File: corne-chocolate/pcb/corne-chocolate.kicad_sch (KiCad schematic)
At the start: 74 parts, among them J1 MJ-4PP-9, J2 Conn_01x04, J3 Conn_01x03, P1 Conn_01x01, P2 Conn_01x01, SW10 SW_PUSH, SW11 SW_PUSH, SW12 SW_PUSH, SW14 SW_PUSH, SW15 SW_PUSH, SW16 SW_PUSH, SW17 SW_PUSH, SW18 SW_PUSH, SW19 SW_PUSH, SW2 SW_PUSH, SW20 SW_PUSH, SW21 SW_PUSH, SW3 SW_PUSH, SW4 SW_PUSH, SW5 SW_PUSH, SW6 SW_PUSH, SW8 SW_PUSH, SW9 SW_PUSH, U1 ProMicro

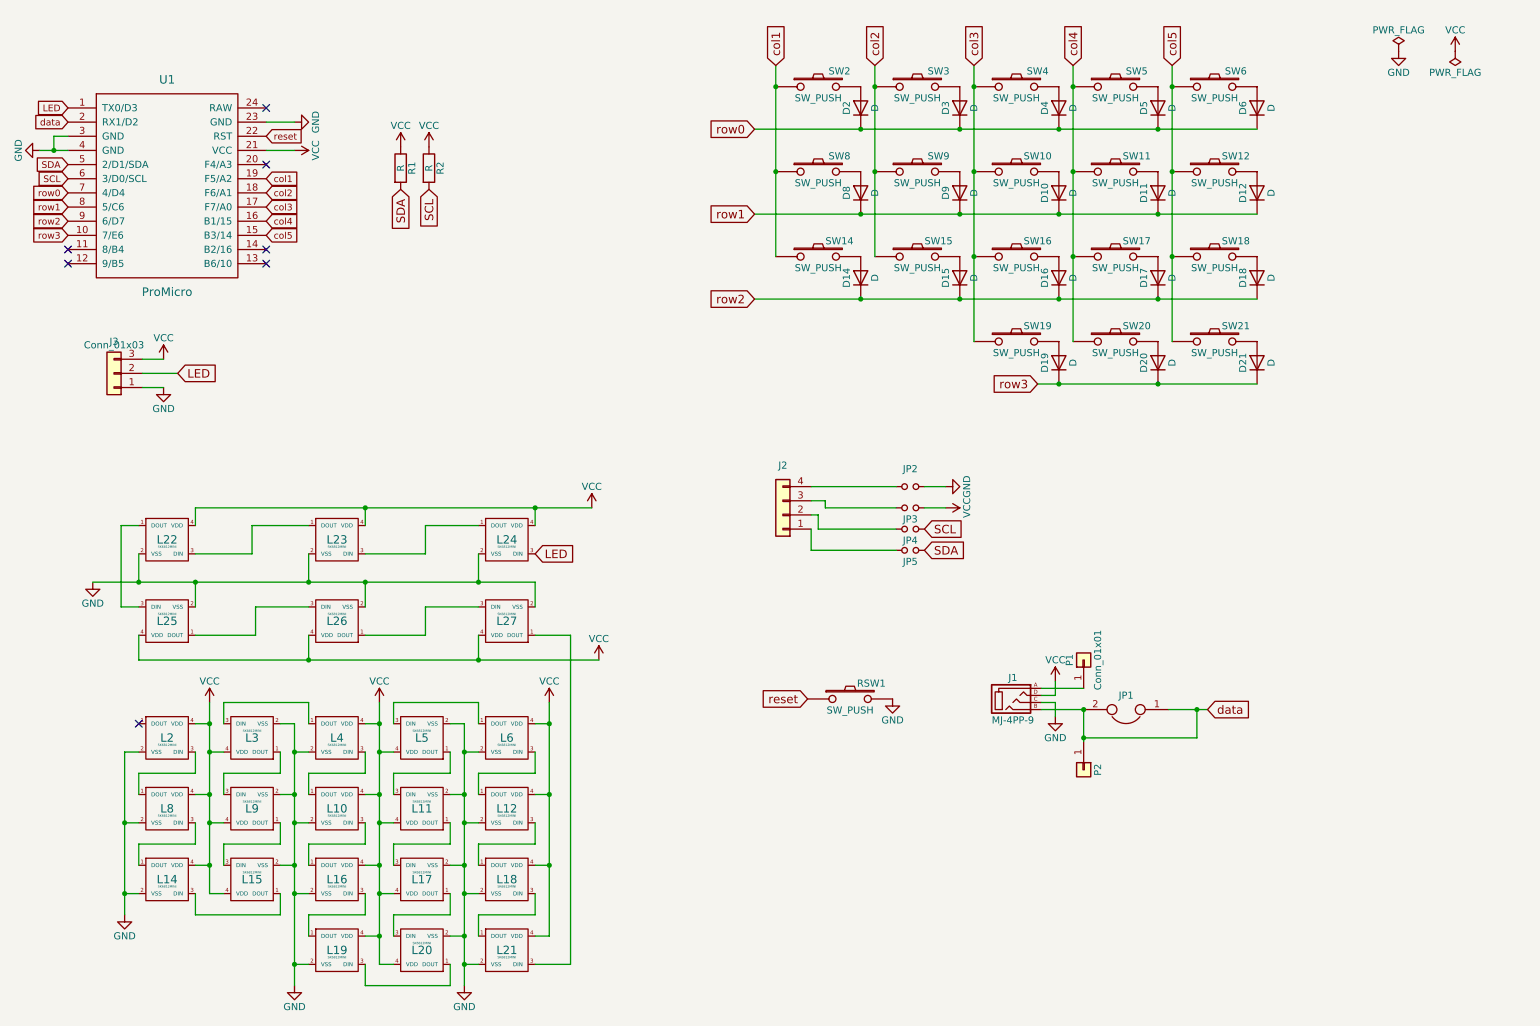
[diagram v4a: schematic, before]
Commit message: pcb with ohspark constraints
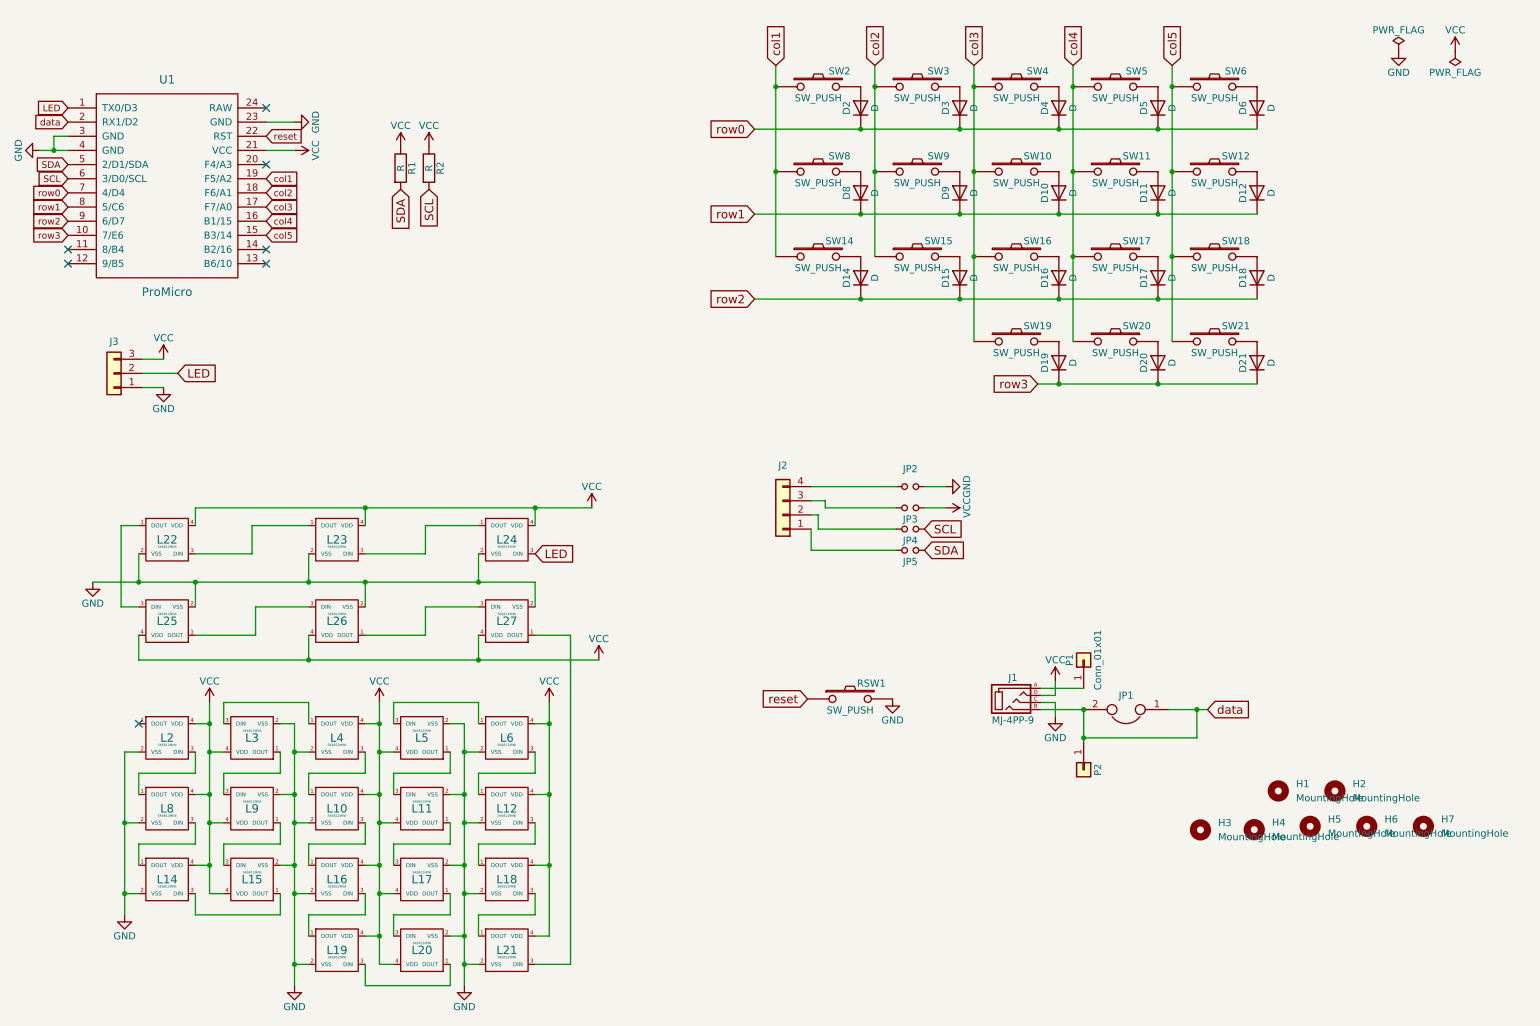
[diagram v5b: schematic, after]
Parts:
- added H1, H2: MountingHole, MountingHole:MountingHole_2.2mm_M2_ISO14580, symbol Mechanical:MountingHole
- added H3, H4, H5, H6, H7: MountingHole, MountingHole:MountingHole_4.3mm_M4_ISO14580, symbol Mechanical:MountingHole
- L10, L11, L12, L14, L15, L16, L17, L18, L19, L2, L20, L21, L3, L4, L5, L6, L8, L9: footprint kbd:SK6812MINI_rev -> kbd:YS-SK6812MINI-E

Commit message: finishes routing
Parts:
- SW10, SW11, SW12, SW14, SW15, SW16, SW17, SW18, SW19, SW2, SW20, SW21, SW3, SW4, SW5, SW6, SW8, SW9: supplier (none) -> Digikey; supplier pn (none) -> 1528-5118-ND
- U1: supplier (none) -> Digikey; supplier pn (none) -> 1568-DEV-15795-ND

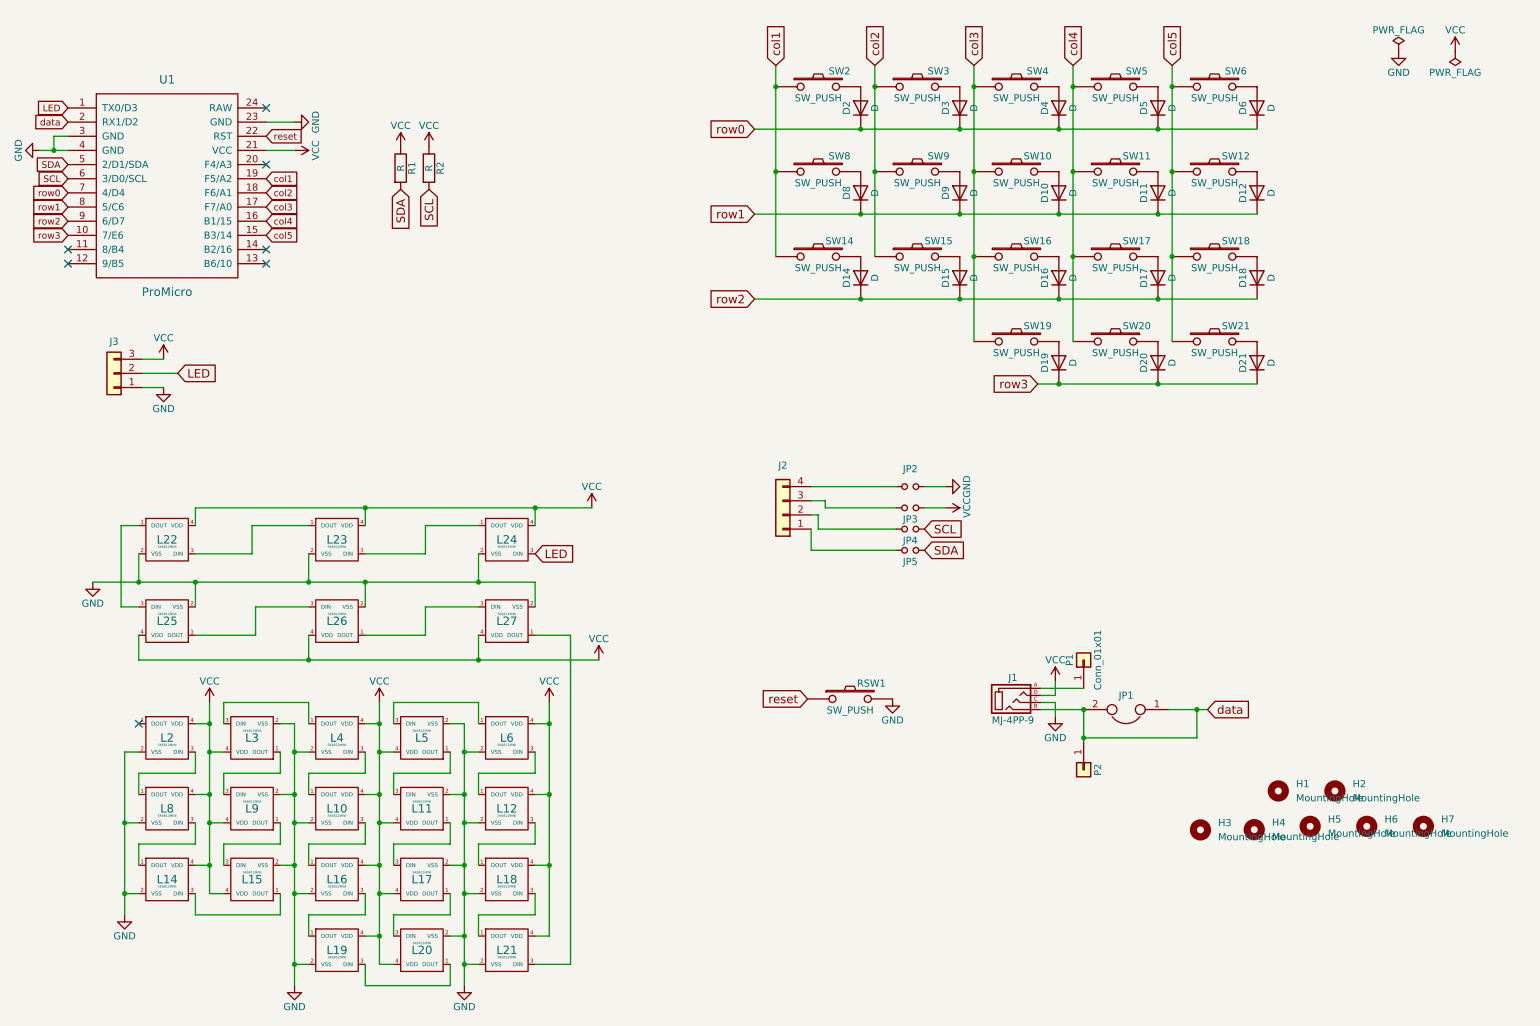
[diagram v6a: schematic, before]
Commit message: updates some footprints
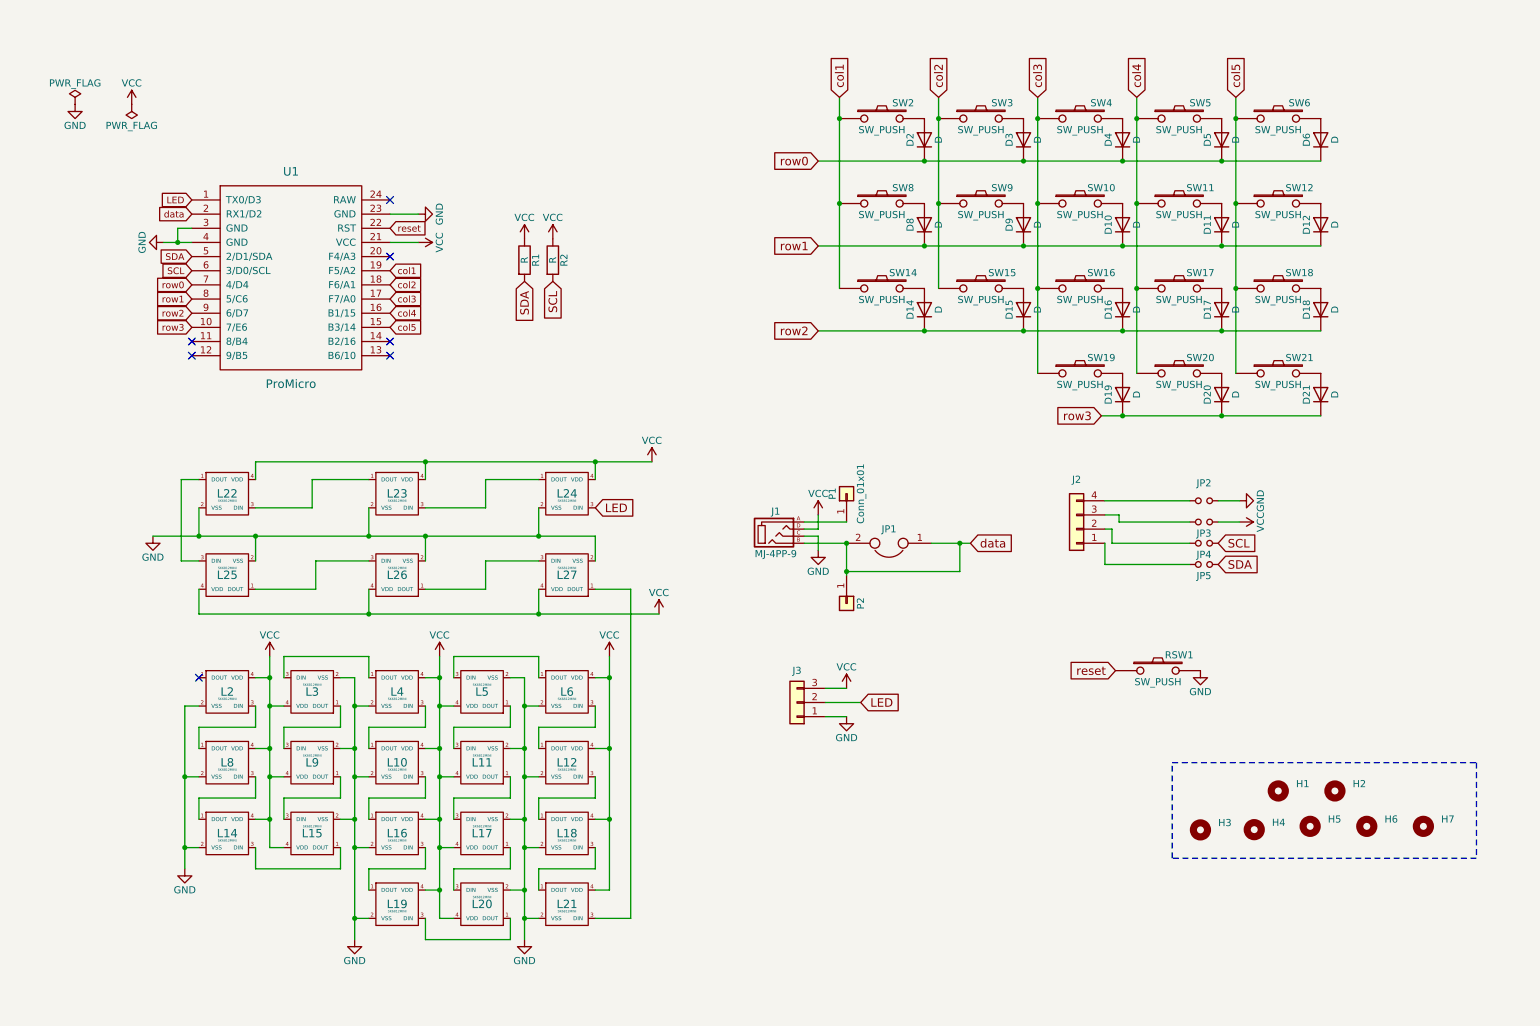
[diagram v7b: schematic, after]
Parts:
- SW14: footprint kbd:ChocV1_V2_Hotswap -> (none); supplier Digikey -> (none); supplier pn 1528-5118-ND -> (none)
- U1: footprint kbd:ProMicro_v2_1side -> (none); supplier Digikey -> (none); supplier pn 1568-DEV-15795-ND -> (none)
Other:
- moved on the sheet: D10, D11, D12, D14, D15, D16, D17, D18, D19, D2, D20, D21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

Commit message: reannotates
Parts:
- removed J3: Conn_01x03, kbd:StripLED_1side, symbol Connector_Generic:Conn_01x03
- removed JP1: Device:Jumper, kbd:Jumper, symbol kbd:Jumper-Device
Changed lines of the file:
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@@
   (junction (at 94.615 145.415) (diameter 0) (color 0 0 0 0)
   )
+  (junction (at 167.64 108.585) (diameter 0) (color 0 0 0 0)
+  )
   (junction (at 79.375 145.415) (diameter 0) (color 0 0 0 0)
   )
@@
   (junction (at 94.615 163.195) (diameter 0) (color 0 0 0 0)
   )
-  (junction (at 187.96 108.585) (diameter 0) (color 0 0 0 0)
-  )
   (junction (at 109.855 170.815) (diameter 0) (color 0 0 0 0)
   )
@@
   (junction (at 201.93 47.625) (diameter 0) (color 0 0 0 0)
   )
-  (junction (at 167.64 108.585) (diameter 0) (color 0 0 0 0)
-  )
   (junction (at 94.615 132.715) (diameter 0) (color 0 0 0 0)
   )
   (junction (at 92.075 107.315) (diameter 0) (color 0 0 0 0)
   )
-  (junction (at 167.64 113.665) (diameter 0) (color 0 0 0 0)
-  )
   (junction (at 217.17 55.245) (diameter 0) (color 0 0 0 0)
   )
@@
     (stroke (width 0) (type default))
   )
-  (wire (pts (xy 167.64 113.665) (xy 167.64 114.3))
+  (wire (pts (xy 167.64 108.585) (xy 167.64 114.3))
     (stroke (width 0) (type default))
   )
@@
     (stroke (width 0) (type default))
   )
-  (wire (pts (xy 167.64 108.585) (xy 167.64 113.665))
-    (stroke (width 0) (type default))
-  )
   (wire (pts (xy 92.075 154.305) (xy 92.075 150.495))
     (stroke (width 0) (type default))
@@
     (stroke (width 0) (type default))
   )
-  (wire (pts (xy 187.96 108.585) (xy 182.88 108.585))
+  (wire (pts (xy 167.64 108.585) (xy 174.625 108.585))
     (stroke (width 0) (type default))
   )
@@
     (stroke (width 0) (type default))
   )
-  (wire (pts (xy 163.83 134.62) (xy 167.64 134.62))
-    (stroke (width 0) (type default))
-  )
   (wire (pts (xy 112.395 170.815) (xy 112.395 167.005))
     (stroke (width 0) (type default))
@@
     (stroke (width 0) (type default))
   )
-  (wire (pts (xy 187.96 113.665) (xy 167.64 113.665))
-    (stroke (width 0) (type default))
-  )
   (wire (pts (xy 76.835 158.115) (xy 79.375 158.115))
     (stroke (width 0) (type default))
@@
     (stroke (width 0) (type default))
   )
-  (wire (pts (xy 163.83 137.16) (xy 170.18 137.16))
-    (stroke (width 0) (type default))
-  )
   (wire (pts (xy 79.375 150.495) (xy 79.375 158.115))
     (stroke (width 0) (type default))
@@
     (stroke (width 0) (type default))
   )
-  (wire (pts (xy 187.96 108.585) (xy 187.96 113.665))
-    (stroke (width 0) (type default))
-  )
   (wire (pts (xy 48.26 97.155) (xy 48.26 111.76))
     (stroke (width 0) (type default))
@@
     (stroke (width 0) (type default))
   )
-  (wire (pts (xy 163.83 139.7) (xy 167.64 139.7))
-    (stroke (width 0) (type default))
-  )
-  (wire (pts (xy 189.865 108.585) (xy 187.96 108.585))
-    (stroke (width 0) (type default))
-  )
   (wire (pts (xy 102.87 97.155) (xy 102.87 102.235))
     (stroke (width 0) (type default))
@@
     )
   )
-  (global_label "data" (shape input) (at 189.865 108.585 0) (fields_autoplaced)
+  (global_label "data" (shape input) (at 174.625 108.585 0) (fields_autoplaced)
     (effects (font (size 1.524 1.524)) (justify left))
-    (property "Intersheetrefs" "${INTERSHEET_REFS}" (at 197.6694 108.585 0)
+    (property "Intersheetrefs" "${INTERSHEET_REFS}" (at 182.4294 108.585 0)
       (effects (font (size 1.27 1.27)) (justify left) hide)
     )
@@
     )
   )
-  (global_label "LED" (shape input) (at 170.18 137.16 0) (fields_autoplaced)
-    (effects (font (size 1.524 1.524)) (justify left))
-    (property "Intersheetrefs" "${INTERSHEET_REFS}" (at 177.1134 137.16 0)
-      (effects (font (size 1.27 1.27)) (justify left) hide)
-    )
-  )
   (global_label "SDA" (shape input) (at 50.165 57.15 180) (fields_autoplaced)
     (effects (font (size 1.1938 1.1938)) (justify right))
@@
     )
   )
-  (symbol (lib_id "Connector_Generic:Conn_01x03") (at 158.75 137.16 180) (unit 1)
-    (in_bom yes) (on_board yes) (dnp no)
-    (property "Reference" "J3" (at 158.75 131.445 0)
-      (effects (font (size 1.27 1.27)))
-    )
-    (property "Value" "Conn_01x03" (at 158.75 132.08 0)
-      (effects (font (size 1.27 1.27)) hide)
-    )
-    (property "Footprint" "kbd:StripLED_1side" (at 158.75 137.16 0)
-      (effects (font (size 1.27 1.27)) hide)
-    )
-    (property "Datasheet" "~" (at 158.75 137.16 0)
-      (effects (font (size 1.27 1.27)) hide)
-    )
-    (property "supplier" "" (at 158.75 137.16 0)
-      (effects (font (size 1.27 1.27)) hide)
-    )
-    (property "supplier pn" "" (at 158.75 137.16 0)
-      (effects (font (size 1.27 1.27)) hide)
-    )
-    (pin "1")
-    (pin "2")
-    (pin "3")
-    (instances
-      (project "corne-chocolate"
-        (path "/b2404ab0-025a-473e-9fbb-0abc932972cf"
-          (reference "J3") (unit 1)
-        )
-      )
-    )
-  )
-  (symbol (lib_id "power:VCC") (at 167.64 134.62 0) (unit 1)
-    (in_bom yes) (on_board yes) (dnp no)
-    (property "Reference" "#PWR024" (at 167.64 138.43 0)
-      (effects (font (size 1.27 1.27)) hide)
-    )
-    (property "Value" "VCC" (at 167.64 130.81 0)
-      (effects (font (size 1.27 1.27)))
-    )
-    (property "Footprint" "" (at 167.64 134.62 0)
-      (effects (font (size 1.27 1.27)) hide)
-    )
-    (property "Datasheet" "" (at 167.64 134.62 0)
-      (effects (font (size 1.27 1.27)) hide)
-    )
-    (pin "1")
-    (instances
-      (project "corne-chocolate"
-        (path "/b2404ab0-025a-473e-9fbb-0abc932972cf"
-          (reference "#PWR024") (unit 1)
-        )
-      )
-    )
-  )
-  (symbol (lib_id "power:GND") (at 167.64 139.7 0) (unit 1)
-    (in_bom yes) (on_board yes) (dnp no)
-    (property "Reference" "#PWR025" (at 167.64 146.05 0)
-      (effects (font (size 1.27 1.27)) hide)
-    )
-    (property "Value" "GND" (at 167.64 143.51 0)
-      (effects (font (size 1.27 1.27)))
-    )
-    (property "Footprint" "" (at 167.64 139.7 0)
-      (effects (font (size 1.27 1.27)) hide)
-    )
-    (property "Datasheet" "" (at 167.64 139.7 0)
-      (effects (font (size 1.27 1.27)) hide)
-    )
-    (pin "1")
-    (instances
-      (project "corne-chocolate"
-        (path "/b2404ab0-025a-473e-9fbb-0abc932972cf"
-          (reference "#PWR025") (unit 1)
-        )
-      )
-    )
-  )
   (symbol (lib_id "kbd:MJ-4PP-9") (at 154.94 106.68 0) (unit 1)
     (in_bom yes) (on_board yes) (dnp no)
@@
         )
       )
-    )
-  )
-  (symbol (lib_id "kbd:Jumper-Device") (at 175.26 108.585 180) (unit 1)
-    (in_bom yes) (on_board yes) (dnp no) (fields_autoplaced)
-    (property "Reference" "JP1" (at 175.26 106.045 0)
-      (effects (font (size 1.27 1.27)))
-    )
-    (property "Value" "Device:Jumper" (at 175.26 106.553 0)
-      (effects (font (size 1.27 1.27)) hide)
-    )
-    (property "Footprint" "kbd:Jumper" (at 175.26 108.585 0)
-      (effects (font (size 1.27 1.27)) hide)
-    )
-    (property "Datasheet" "" (at 175.26 108.585 0)
-      (effects (font (size 1.27 1.27)) hide)
-    )
-    (property "supplier" "" (at 175.26 108.585 0)
-      (effects (font (size 1.27 1.27)) hide)
-    )
-    (property "supplier pn" "" (at 175.26 108.585 0)
-      (effects (font (size 1.27 1.27)) hide)
-    )
-    (pin "1")
-    (pin "2")
-    (instances
-      (project "corne-chocolate"
-        (path "/b2404ab0-025a-473e-9fbb-0abc932972cf"
-          (reference "JP1") (unit 1)
-        )
-      )
